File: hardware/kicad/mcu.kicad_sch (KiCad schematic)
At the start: 34 parts, among them J3 SWD, J4 UART, J5 Reset_Switch, SW2 PEC11R-4220F-S0024, U6 OLED, U7 STM32F072CBTx, U8 PCT2075GV, Y1 Crystal_8MHz

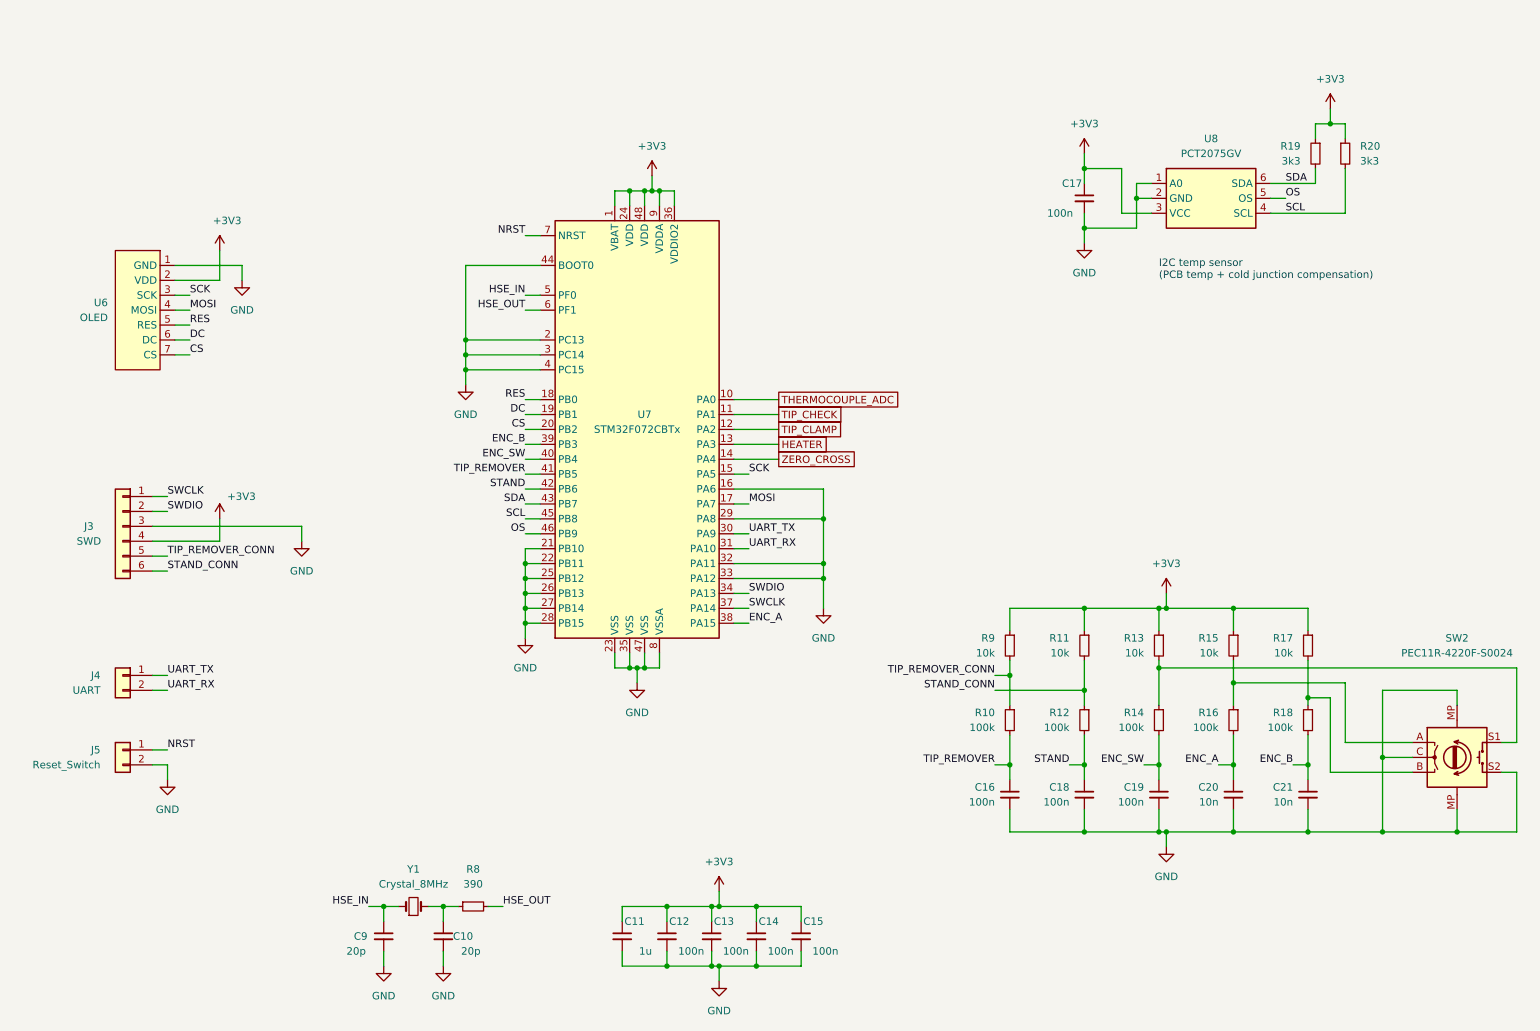
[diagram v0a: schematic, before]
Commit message: [HW] Add: - Tag Connect Debug connector - USB & I2C breakout - GND pin to UART breakout
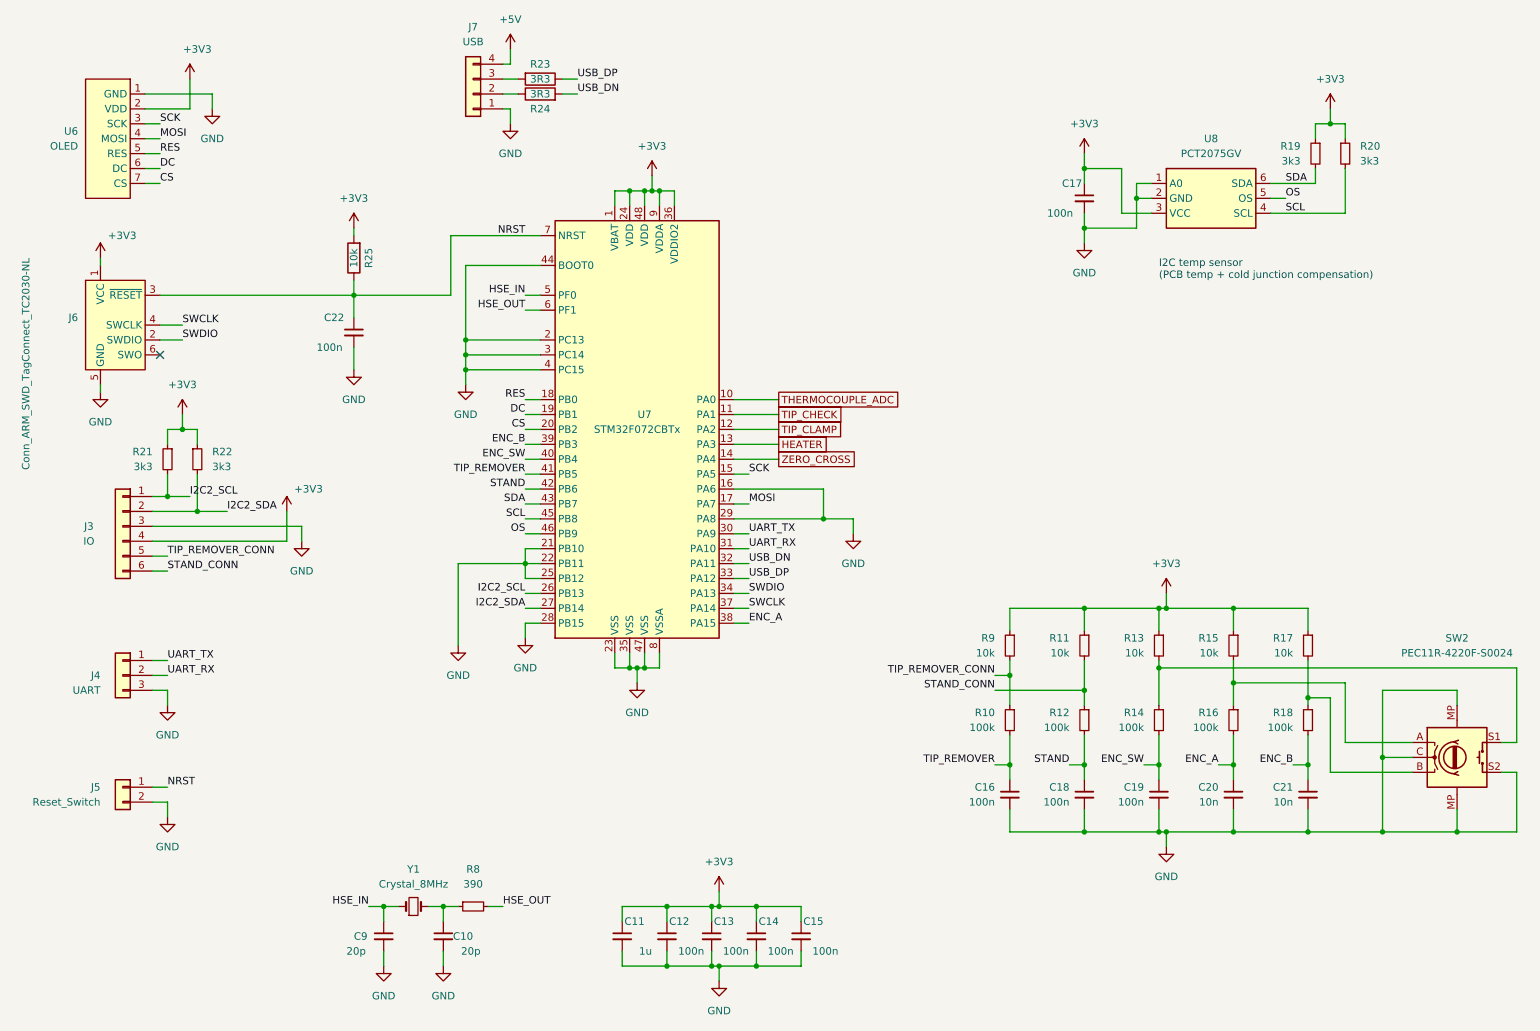
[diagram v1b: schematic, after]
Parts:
- added C22: 100n, Capacitor_SMD:C_0603_1608Metric, symbol Device:C_Small
- added J6: Conn_ARM_SWD_TagConnect_TC2030-NL, Connector:Tag-Connect_TC2030-IDC-NL_2x03_P1.27mm_Vertical, symbol Connector:Conn_ARM_SWD_TagConnect_TC2030-NL
- added J7: USB, Connector_PinSocket_2.54mm:PinSocket_1x04_P2.54mm_Vertical, symbol Connector_Generic:Conn_01x04
- added R21, R22: 3k3, Resistor_SMD:R_0603_1608Metric, symbol Device:R_Small
- added R23, R24: 3R3, Resistor_SMD:R_0603_1608Metric, symbol Device:R
- added R25: 10k, Resistor_SMD:R_0603_1608Metric, symbol Device:R
- C10, C16, C17, C18, C19, C20, C21, C9: footprint Capacitor_SMD:C_0805_2012Metric -> Capacitor_SMD:C_0603_1608Metric
- J3: value SWD -> IO; footprint Connector_IDC:IDC-Header_2x03_P2.54mm_Vertical -> Connector_PinHeader_2.54mm:PinHeader_2x03_P2.54mm_Vertical
- J4: footprint Connector_PinSocket_2.54mm:PinSocket_1x02_P2.54mm_Vertical -> Connector_PinSocket_2.54mm:PinSocket_1x03_P2.54mm_Vertical; symbol Connector_Generic:Conn_01x02 -> Connector_Generic:Conn_01x03
- R10, R11, R12, R13, R14, R15, R16, R17, R18, R19, R20, R8, R9: footprint Resistor_SMD:R_0805_2012Metric -> Resistor_SMD:R_0603_1608Metric
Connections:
- net +3V3: now also J6.1 (VCC), R21.1, R22.1, R25.2
- net GND: now also J4.3 (Pin_3), C22.2, J6.5 (GND), J7.1 (Pin_1); no longer U7.26 (PB13), U7.27 (PB14), U7.32 (PA11), U7.33 (PA12)
- net NRST: now also C22.1, J6.3 (~{RESET}), R25.1
- net SWCLK: now also J6.4 (SWCLK); no longer J3.1 (Pin_1)
- net SWDIO: now also J6.2 (SWDIO); no longer J3.2 (Pin_2)
- new net: J7.2 (Pin_2), R24.1
- new net: J7.3 (Pin_3), R23.2
- new net +5V: J7.4 (Pin_4)
- new net I2C2_SCL: J3.1 (Pin_1), R21.2, U7.26 (PB13)
- new net I2C2_SDA: J3.2 (Pin_2), R22.2, U7.27 (PB14)
- new net USB_DN: R24.2, U7.32 (PA11)
- new net USB_DP: R23.1, U7.33 (PA12)
- no-connect marks 0 -> 1
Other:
- title: OpenSolder Station Schematic -> Marcs OpenSolder Station Schematic
- moved on the sheet: J5, U6
